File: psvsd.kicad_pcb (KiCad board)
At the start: 2 copper layers, 30 x 33.2 mm, 32 parts, among them J1 MEM2075-00-140-01-A, U1 RP2040, U2 3.3V, U4 W25Q32JVZP, X1 ABM8-272-T3

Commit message: Add UART and SWDIO debug headers (plus delete some accidental junk files)
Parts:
- added J2: BM04B-SURS-TF, Connector_JST:JST_SUR_BM04B-SURS-TF_1x04-1MP_P0.80mm_Vertical, F.Cu at (161.9, 105.0)
- added J3: BM05B-SURS-TF, Connector_JST:JST_SUR_BM05B-SURS-TF_1x05-1MP_P0.80mm_Vertical, F.Cu at (135.1, 103.0)
- added J4: BM05B-SURS-TF, Connector_JST:JST_SUR_BM05B-SURS-TF_1x05-1MP_P0.80mm_Vertical, F.Cu at (135.1, 111.4)
- moved C10 1.80 mm to (136.9, 95.0)
- moved C9 1.80 mm to (136.9, 98.8)
- moved U2 1.80 mm to (139.5, 96.2)
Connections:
- U$1 pad 10: unconnected-(U$1A-UART_KERMIT_CTS-Pad10) -> UART_KER_TX
- U$1 pad 12: unconnected-(U$1A-UART_KERMIT_TX-Pad12) -> UART_KER_CTS
- U$1 pad 14: unconnected-(U$1A-UART_KERMIT_RX-Pad14) -> UART_KER_RFR
- U$1 pad 18: unconnected-(U$1A-UART_SYSCON_RX-Pad18) -> UART_SYS_RFR
- U$1 pad 20: unconnected-(U$1A-UART_SYSCON_TX-Pad20) -> UART_SYS_CTS
- U$1 pad 38: unconnected-(U$1A-UART_SYSCON_RFR-Pad38) -> UART_SYS_RX
- U$1 pad 40: unconnected-(U$1A-UART_SYSCON_CTS-Pad40) -> UART_SYS_TX
- U$1 pad 8: unconnected-(U$1A-UART_KERMIT_RFR-Pad8) -> UART_KER_RX
- U1 pad 24: unconnected-(U1-SWCLK-Pad24) -> /psvsd-2040/SWCLK
- U1 pad 25: unconnected-(U1-SWDIO-Pad25) -> /psvsd-2040/SWDIO
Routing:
- net /psvsd-2040/SWDIO: track 0.00 -> 10.8 mm, vias 0 -> 1
- net /psvsd-2040/SWCLK: track 0.00 -> 10.4 mm, vias 0 -> 1
- net VDD33: track 25.9 -> 22.6 mm

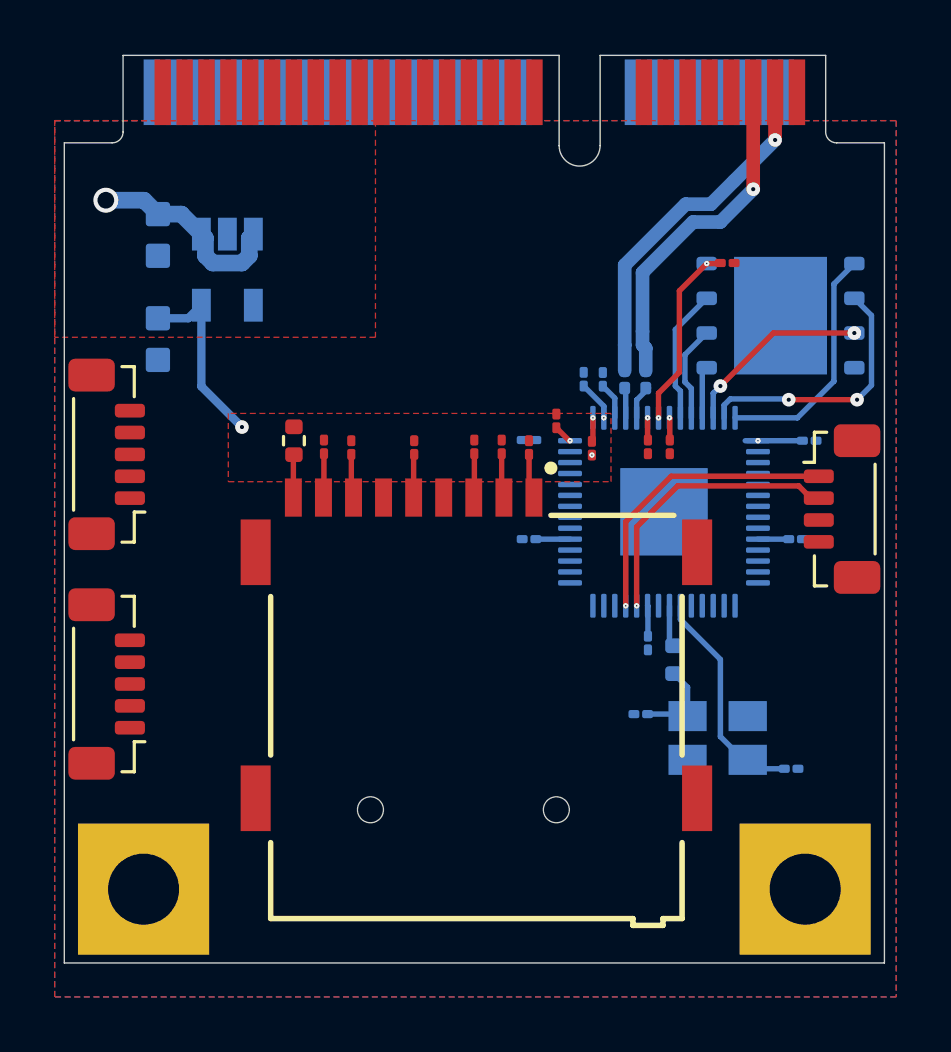
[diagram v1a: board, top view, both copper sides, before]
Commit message: Connect SD slot and fix pull-up issue
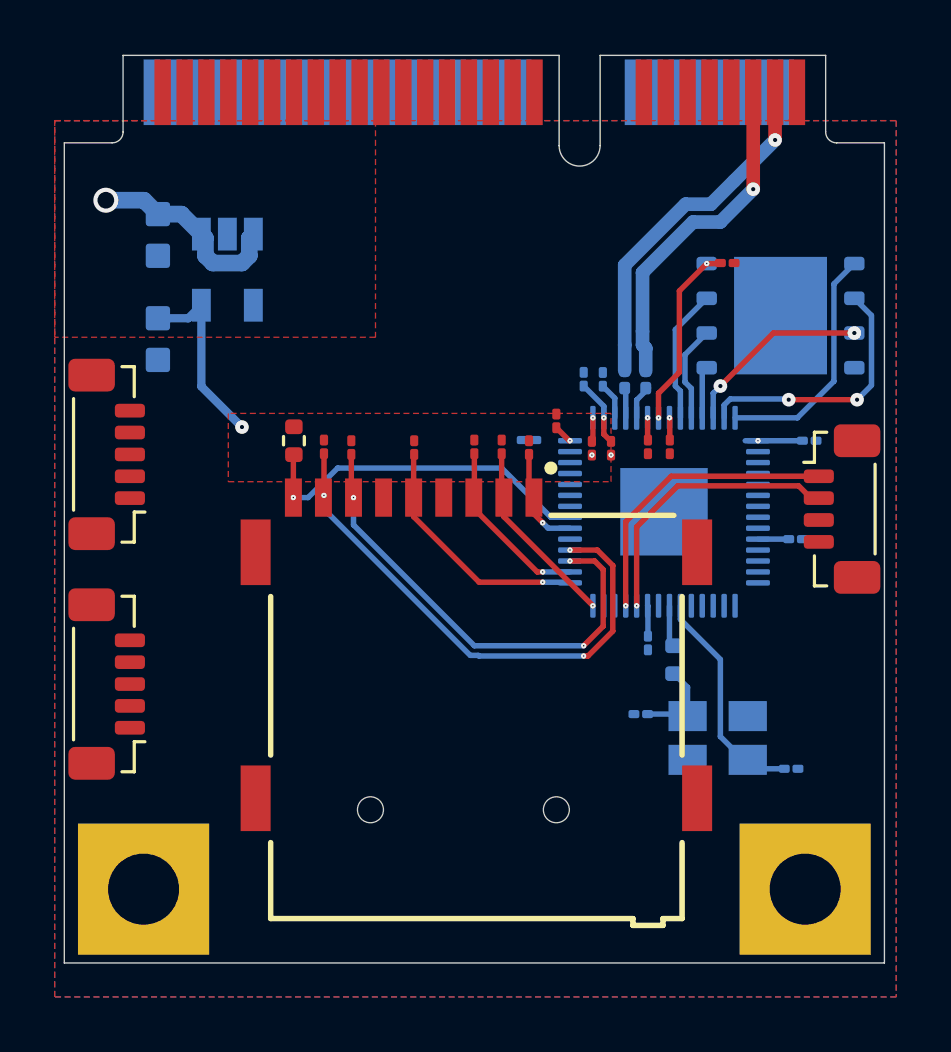
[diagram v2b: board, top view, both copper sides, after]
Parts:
- C6: moved to F.Cu
- R2, R3: value ?? -> 27
- moved C6 4.48 mm to (153.5, 102.8), turned to -90 degrees
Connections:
- net QSPI_SCLK renamed /psvsd-2040/QSPI_SCLK
- net QSPI_SD0 renamed /psvsd-2040/QSPI_SD0
- net QSPI_SD1 renamed /psvsd-2040/QSPI_SD1
- net QSPI_SD2 renamed /psvsd-2040/QSPI_SD2
- net QSPI_SD3 renamed /psvsd-2040/QSPI_SD3
- net QSPI_SS renamed /psvsd-2040/QSPI_SS
- J1 pad P1: Net-(J1-DAT2) -> /psvsd-2040/SD_D2
- J1 pad P2: Net-(J1-CD/DAT3) -> /psvsd-2040/SD_D3/CS
- J1 pad P3: Net-(J1-CMD) -> /psvsd-2040/SD_CMD
- J1 pad P5: Net-(J1-CLK) -> /psvsd-2040/SD_CLK
- J1 pad P7: Net-(J1-DAT0) -> /psvsd-2040/SD_D0
- J1 pad P8: Net-(J1-DAT1) -> /psvsd-2040/SD_D1
- J3 pad 1: UART_KER_RFR -> UART_KER_RX
- J3 pad 2: UART_KER_CTS -> UART_KER_TX
- J3 pad 3: UART_KER_TX -> UART_KER_CTS
- J3 pad 4: UART_KER_RX -> UART_KER_RFR
- J4 pad 1: UART_SYS_RFR -> UART_SYS_RX
- J4 pad 2: UART_SYS_CTS -> UART_SYS_TX
- J4 pad 3: UART_SYS_TX -> UART_SYS_CTS
- J4 pad 4: UART_SYS_RX -> UART_SYS_RFR
- R4 pad 2: Net-(J1-CLK) -> /psvsd-2040/SD_CLK
- R5 pad 2: Net-(J1-CMD) -> /psvsd-2040/SD_CMD
- R6 pad 2: Net-(J1-DAT0) -> /psvsd-2040/SD_D0
- R7 pad 2: Net-(J1-DAT1) -> /psvsd-2040/SD_D1
- R8 pad 2: Net-(J1-DAT2) -> /psvsd-2040/SD_D2
- R9 pad 2: Net-(J1-CD/DAT3) -> /psvsd-2040/SD_D3/CS
- U$1 pad 10: UART_KER_TX -> UART_KER_CTS
- U$1 pad 12: UART_KER_CTS -> UART_KER_TX
- U$1 pad 14: UART_KER_RFR -> UART_KER_RX
- U$1 pad 18: UART_SYS_RFR -> UART_SYS_RX
- U$1 pad 20: UART_SYS_CTS -> UART_SYS_TX
- U$1 pad 38: UART_SYS_RX -> UART_SYS_RFR
- U$1 pad 40: UART_SYS_TX -> UART_SYS_CTS
- U$1 pad 8: UART_KER_RX -> UART_KER_RFR
- U1 pad 28: unconnected-(U1-GPIO17-Pad28) -> /psvsd-2040/SD_D3/CS
- U1 pad 29: unconnected-(U1-GPIO18-Pad29) -> /psvsd-2040/SD_CLK
- U1 pad 30: unconnected-(U1-GPIO19-Pad30) -> /psvsd-2040/SD_CMD
- U1 pad 31: unconnected-(U1-GPIO20-Pad31) -> /psvsd-2040/SD_D0
- U1 pad 32: unconnected-(U1-GPIO21-Pad32) -> /psvsd-2040/SD_D1
- U1 pad 34: unconnected-(U1-GPIO22-Pad34) -> /psvsd-2040/SD_D2
- U1 pad 35: unconnected-(U1-GPIO23-Pad35) -> /psvsd-2040/SD_CD
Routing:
- net /psvsd-2040/SD_D1: track 0.00 -> 19.5 mm, vias 0 -> 3
- net /psvsd-2040/SD_D0: track 0.00 -> 17.3 mm, vias 0 -> 3
- net /psvsd-2040/SD_CD: track 1.58 -> 12.9 mm, vias 0 -> 1
- net /psvsd-2040/SD_CLK: track 0.00 -> 9.01 mm, vias 0 -> 1
- net /psvsd-2040/SD_D3/CS: track 0.00 -> 6.94 mm, vias 0 -> 1
- net /psvsd-2040/SD_CMD: track 0.00 -> 6.94 mm, vias 0 -> 1
- net /psvsd-2040/SD_D2: track 0.00 -> 3.79 mm, vias 0 -> 1
- net Net-(J1-DAT2): track 1.65 -> 0.00 mm
- net Net-(J1-CD/DAT3): track 1.64 -> 0.00 mm
- net Net-(J1-DAT1): track 1.61 -> 0.00 mm
- net Net-(J1-CMD): track 1.61 -> 0.00 mm
- net Net-(J1-DAT0): track 1.61 -> 0.00 mm
- net Net-(J1-CLK): track 1.59 -> 0.00 mm
- net GND: vias 1 -> 2

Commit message: Connect Kermit and Syscon debug headers
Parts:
- moved R10 0.30 mm to (141.9, 102.8)
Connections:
- J3 pad 1: UART_KER_RX -> UART_KER_RFR
- J3 pad 2: UART_KER_TX -> UART_KER_CTS
- J3 pad 3: UART_KER_CTS -> UART_KER_TX
- J3 pad 4: UART_KER_RFR -> UART_KER_RX
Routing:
- net UART_SYS_RX: track 0.00 -> 30.4 mm, vias 0 -> 1
- net UART_SYS_TX: track 0.00 -> 29.3 mm, vias 0 -> 1
- net UART_KER_RFR: track 0.00 -> 28.6 mm, vias 0 -> 1
- net UART_KER_CTS: track 0.00 -> 27.2 mm, vias 0 -> 1
- net UART_KER_TX: track 0.00 -> 26.3 mm, vias 0 -> 1
- net UART_KER_RX: track 0.00 -> 25.3 mm, vias 0 -> 1
- net UART_SYS_CTS: track 0.00 -> 24.5 mm, vias 0 -> 1
- net UART_SYS_RFR: track 0.00 -> 24.2 mm, vias 0 -> 1
- net VDD33: track 22.3 -> 24.2 mm

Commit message: Fix wrong resistor package
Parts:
- C10, C9: footprint Footprints:C0603_464 -> Capacitor_SMD:C_01005_0402Metric
- R10: footprint Resistor_SMD:R_0402_1005Metric -> Resistor_SMD:R_01005_0402Metric
- moved C10 1.98 mm to (135.0, 94.5), turned to -90 degrees
- moved C9 0.81 mm to (136.7, 98.0)
- moved R10 0.08 mm to (141.9, 102.7)

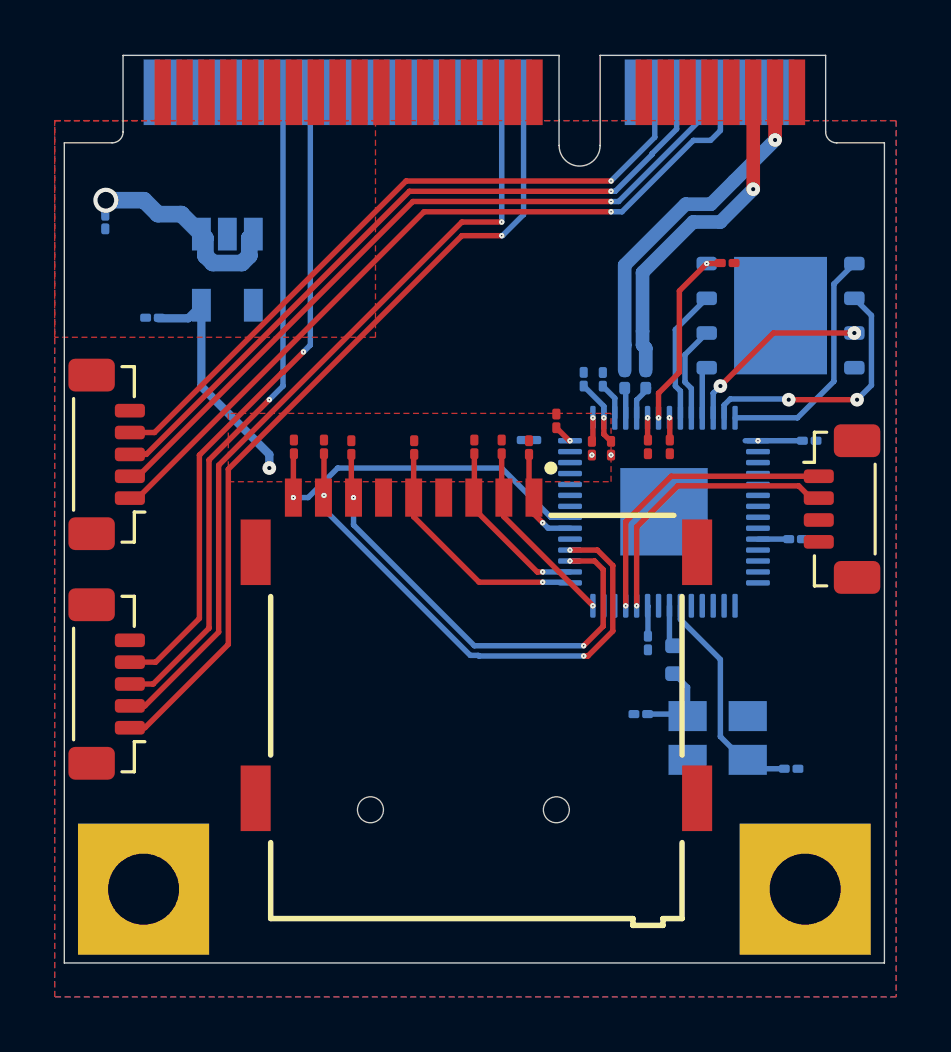
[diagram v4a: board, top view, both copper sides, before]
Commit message: Improved layout to reduce reflections
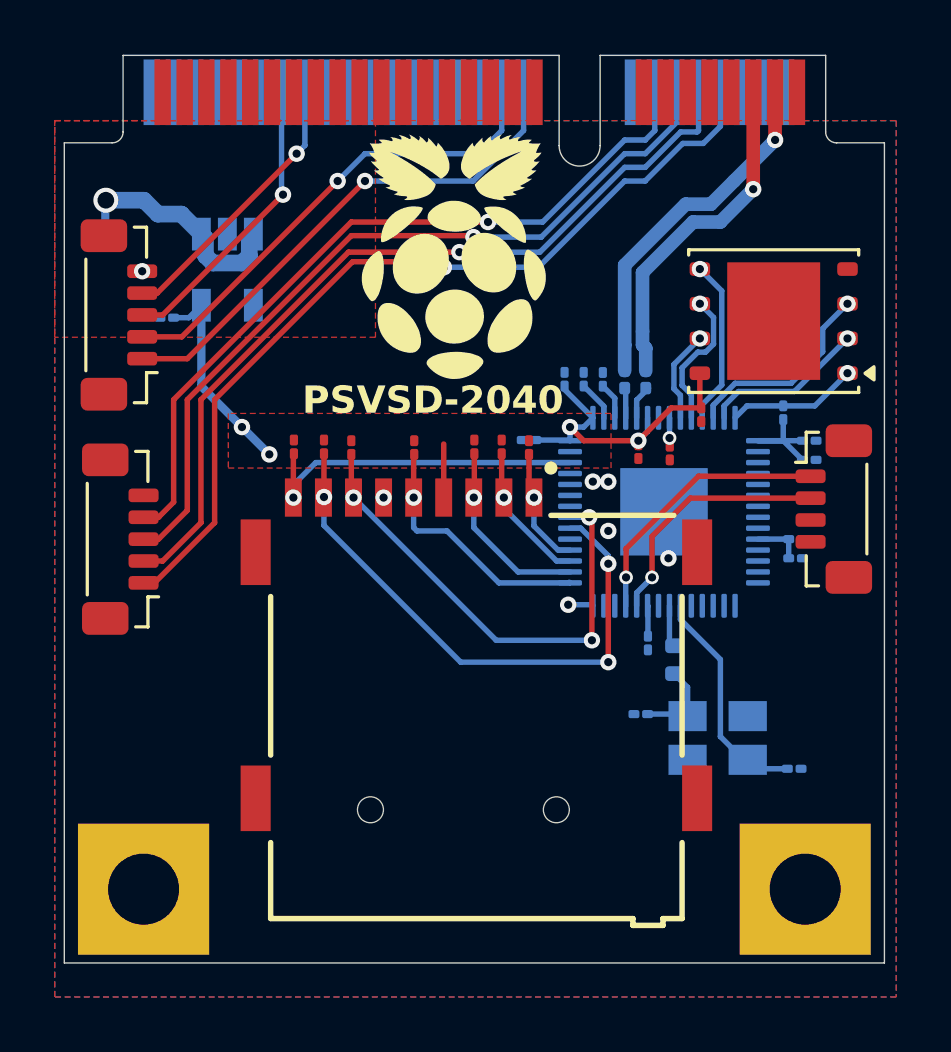
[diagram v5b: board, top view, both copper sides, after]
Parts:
- added G***: LOGO, Images:Raspberry Pi, F.Cu at (148.0, 95.8)
- added G***: LOGO, Images:misuzu_7, B.Cu at (143.2, 110.4)
- added R11: 2k, Resistor_SMD:R_01005_0402Metric, B.Cu at (159.8, 101.5)
- C4, C6, C7: moved to B.Cu
- U4: moved to F.Cu
- moved J4 13.5 mm to (135.5, 97.9)
- moved C7 8.47 mm to (160.2, 106.8), turned to 0 degrees
- moved C6 7.26 mm to (160.8, 103.2), turned to 0 degrees
- moved C15 5.63 mm to (156.8, 101.5), turned to -90 degrees
- moved J3 3.14 mm to (135.6, 106.1)
- moved C4 1.55 mm to (151.8, 100.2)
- moved C9 0.53 mm to (137.2, 98.0)
- moved C1 0.39 mm to (154.5, 102.9)
- moved U4 0.32 mm to (159.4, 98.1)
- moved J2 0.30 mm to (161.7, 105.0)
- moved C12 0.23 mm to (155.7, 103.0)
- moved C17 0.11 mm to (160.2, 114.5)
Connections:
- J1 pad P4: GND -> VDD33
- U1 pad 28: /psvsd-2040/SD_D3/CS -> unconnected-(U1-GPIO17-Pad28)
- U1 pad 31: /psvsd-2040/SD_D0 -> /psvsd-2040/SD_D3/CS
- U1 pad 32: /psvsd-2040/SD_D1 -> /psvsd-2040/SD_D2
- U1 pad 34: /psvsd-2040/SD_D2 -> /psvsd-2040/SD_D1
- U1 pad 35: /psvsd-2040/SD_CD -> /psvsd-2040/SD_D0
- U1 pad 40: unconnected-(U1-GPIO28/ADC2-Pad40) -> /psvsd-2040/SD_CD
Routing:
- net UART_SYS_RFR: track 24.2 -> 10.4 mm
- net UART_SYS_CTS: track 24.5 -> 10.8 mm
- net UART_SYS_RX: track 30.4 -> 18.8 mm
- net UART_SYS_TX: track 29.3 -> 17.7 mm
- net VDD33: track 24.2 -> 29.4 mm, vias 8 -> 4
- net /psvsd-2040/QSPI_SD0: track 1.90 -> 6.07 mm, vias 0 -> 1
- net /psvsd-2040/QSPI_SS: track 8.78 -> 4.79 mm, vias 0 -> 1
- net /psvsd-2040/QSPI_SD1: track 9.62 -> 5.97 mm, vias 2 -> 1
- net UART_KER_CTS: track 27.2 -> 30.9 mm
- net UART_KER_RFR: track 28.6 -> 32.1 mm
- net UART_KER_TX: track 26.3 -> 29.3 mm
- net UART_KER_RX: track 25.3 -> 28.2 mm
- net /psvsd-2040/SD_D3/CS: track 6.94 -> 5.28 mm
- net /psvsd-2040/QSPI_SCLK: track 3.53 -> 5.16 mm, vias 0 -> 1
- net /psvsd-2040/QSPI_SD3: track 4.92 -> 3.39 mm, vias 0 -> 1
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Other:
- board text added: "PSVSD-2040"
- board text added: "Χανια, Κρητη Καλοκαιρη 2026"

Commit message: Added external 3.3v supply for debug (with backflow diodes)
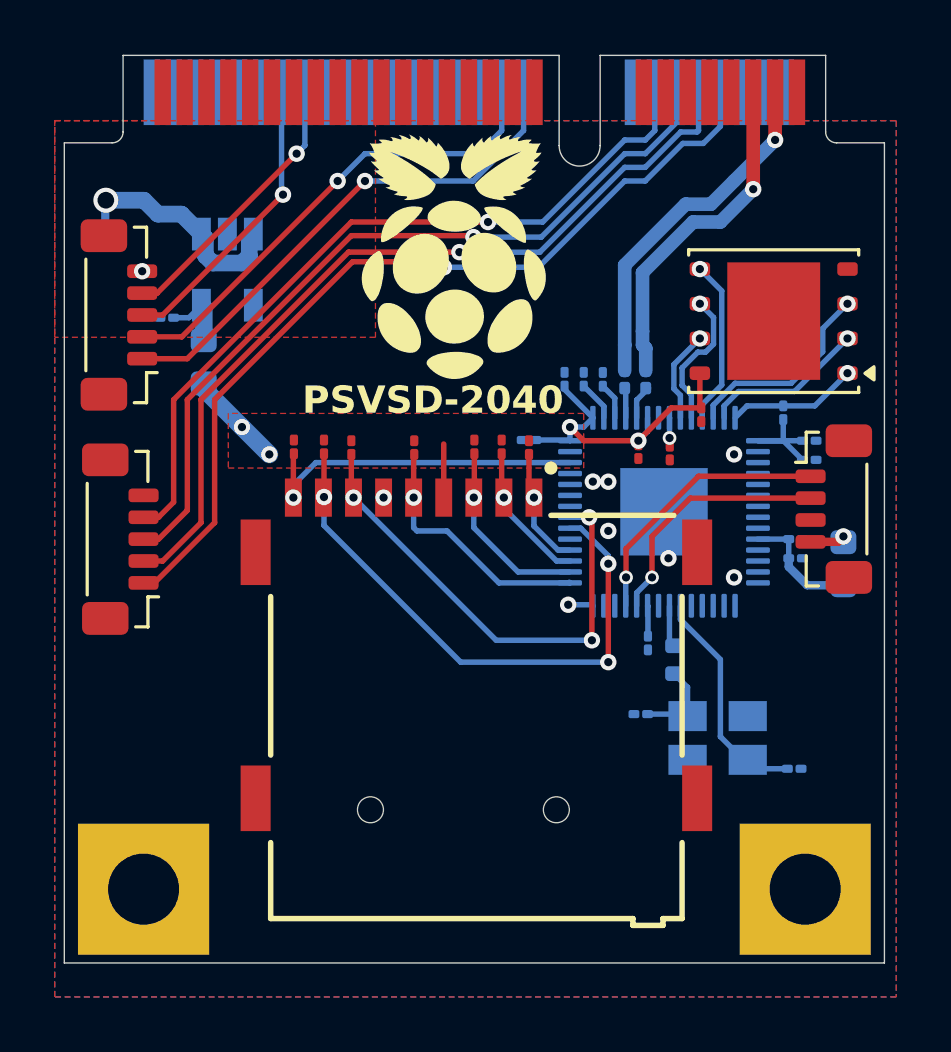
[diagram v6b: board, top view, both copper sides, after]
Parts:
- removed the G*** at (143.2, 110.4)
- added D1: CD0603-B0340R, Diode_SMD:D_0603_1608Metric, B.Cu at (162.0, 107.0)
- added D2: CD0603-B0340R, Diode_SMD:D_0603_1608Metric, B.Cu at (138.6, 99.6)
- R11: value 2k -> 10k
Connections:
- C9 pad 1: VDD33 -> Net-(D2-A)
- J2 pad 4: GND -> Net-(D1-A)
- U2 pad 5: VDD33 -> Net-(D2-A)
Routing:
- net Net-(D2-A): track 0.00 -> 2.52 mm
- net VDD33: track 29.4 -> 27.9 mm
- net Net-(D1-A): track 0.00 -> 1.28 mm, vias 0 -> 1
- net GND: vias 6 -> 8

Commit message: Increased size of footprints to comply with more fab houses.
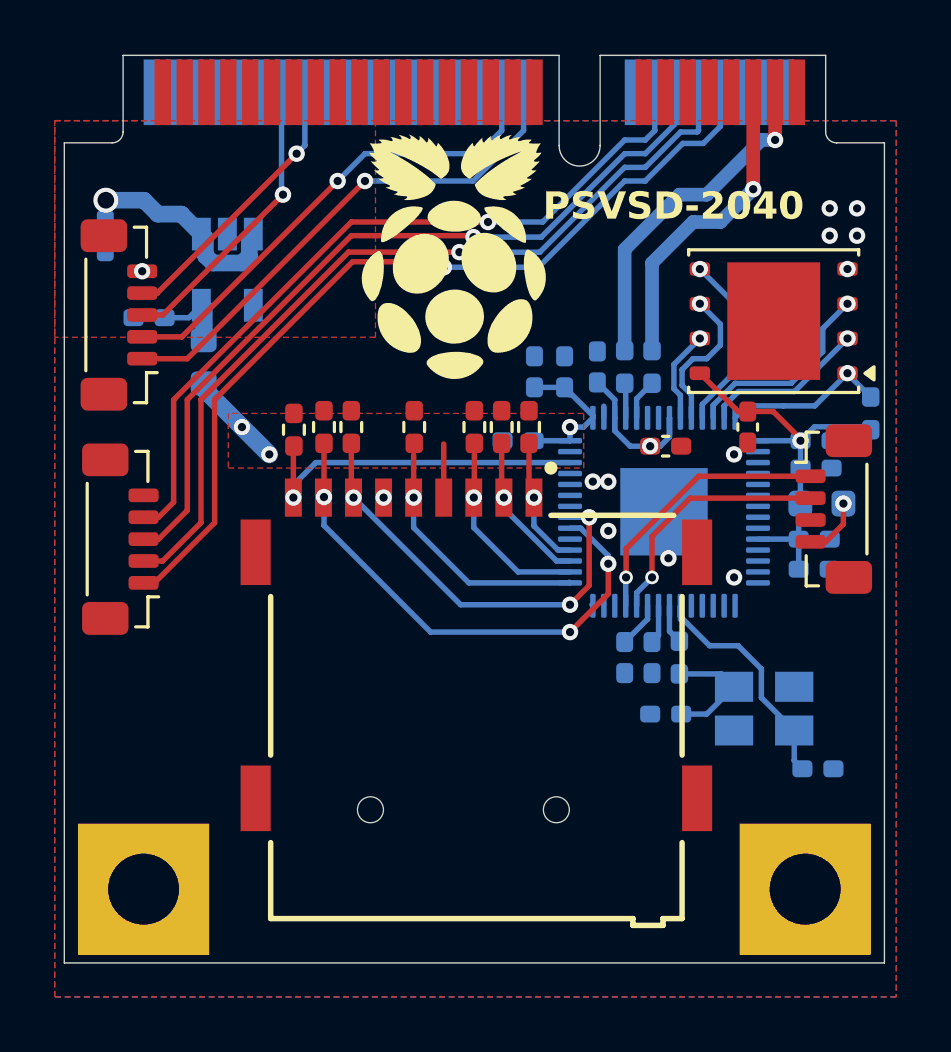
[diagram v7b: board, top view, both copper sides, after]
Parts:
- C1, C10, C11, C12, C13, C14, C16, C17, C2, C3, C4, C5, C6, C7, C9: footprint Capacitor_SMD:C_01005_0402Metric -> Capacitor_SMD:C_0402_1005Metric_Pad0.74x0.62mm_HandSolder
- C15: footprint Capacitor_SMD:C_01005_0402Metric -> Capacitor_SMD:C_0402_1005Metric_Pad0.74x0.62mm_HandSolder; moved to B.Cu
- R1: footprint Resistor_SMD:R_0402_1005Metric -> Resistor_SMD:R_0402_1005Metric_Pad0.72x0.64mm_HandSolder
- R10, R11, R4, R5, R6, R7, R8, R9: footprint Resistor_SMD:R_01005_0402Metric -> Resistor_SMD:R_0402_1005Metric_Pad0.72x0.64mm_HandSolder
- R2, R3: footprint Resistor_SMD:R_0201_0603Metric -> Resistor_SMD:R_0402_1005Metric_Pad0.72x0.64mm_HandSolder
- moved C15 9.06 mm to (155.0, 110.4)
- moved C1 4.10 mm to (158.5, 102.0)
- moved R11 3.20 mm to (163.0, 101.5)
- moved D1 2.34 mm to (161.2, 104.8), turned to 0 degrees
- moved X1 2.01 mm to (159.1, 112.3)
- moved C4 1.13 mm to (150.7, 100.0)
- moved C11 1.00 mm to (154.0, 110.4)
- moved C16 0.91 mm to (155.5, 112.5)
- moved C17 0.87 mm to (161.1, 114.5)
- moved C7 0.79 mm to (160.9, 107.2)
- moved C14 0.75 mm to (151.8, 100.0)
- moved R4 0.75 mm to (146.3, 102.0)
- moved R6 0.75 mm to (144.0, 102.0)
- moved R8 0.75 mm to (150.5, 102.0)
- moved R5 0.72 mm to (148.5, 102.0)
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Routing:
- net Net-(U1-VREG_VOUT): track 3.50 -> 7.42 mm
- net /psvsd-2040/SD_D1: track 20.8 -> 18.5 mm
- net /psvsd-2040/SD_D0: track 17.7 -> 15.5 mm
- net /psvsd-2040/QSPI_SS: track 4.79 -> 6.01 mm
- net Net-(C16-Pad2): track 3.55 -> 4.54 mm
- net unconnected-(U1-GPIO17-Pad28): track 0.99 -> 0.05 mm, vias 1 -> 0
- net USB_P: track 12.5 -> 11.6 mm
- net Net-(D1-A): track 1.28 -> 2.02 mm
- net /psvsd-2040/XIN: track 8.37 -> 8.92 mm
- net GND: vias 8 -> 13
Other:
- board text removed: "Χανια, Κρητη Καλοκαιρη 2026"
